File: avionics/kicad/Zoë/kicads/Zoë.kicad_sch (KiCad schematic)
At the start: 52 parts, among them SW1 SW_DIP_x02, X2Y-CAN 4.7nF_X2Y, X2Y-RS485 4.7nF_X2Y

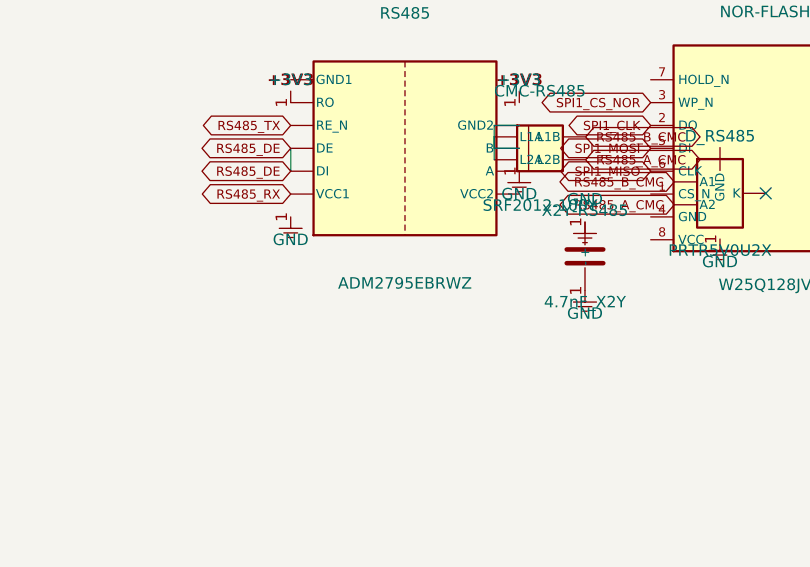
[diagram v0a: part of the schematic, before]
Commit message: Fleet trust module (MCU+TPM+isolated CAN-FD+RS-485) across new CAN-PERIPH-GW-1 board, Jayne, Kaylee, Emma; ISOW1412 swap on Wash/Zoë
- New stackable CAN-PERIPH-GW-1 gateway board (N_STACKS param): MSPM0G3507
  + SLB9670 TPM + ISOW1044BDFMR isolated CAN-FD + ISOW1412 isolated RS-485,
  informed by the public VimDrones ap_periph_pico/ESC S50 concept (no
  VimDrones GPL-3.0 source copied). PCB freerouted via the Specctra DSN/SES
  bridge (tools/export-specctra-dsn.py + import-specctra-ses.py +
  freerouting 2.2.4); user's manual footprint packing preserved.
- Jayne: added ISOW1412 isolated RS-485 (Section H); MSPM0G3507 pinmux
  re-verified against the real datasheet for all new assignments.
- Kaylee: full trust module added via non-destructive schematic injection
  (inject_kaylee_trust_module.py) -- gen_kaylee.py itself has drifted from
  the checked-in file and is not safe to regenerate from (tracked as an
  open item).
- Emma: SLB9670 TPM added via a dedicated header (inject_emma_tpm.py); no
  separate CAN/RS-485 needed, reaches the bus via Zoë's P1/P2 link.
- Fleet-wide ADM2795E -> ISOW1412 (integrated isolated DC-DC). While
  swapping Wash/Zoë, fixed their pre-existing broken ADM2795EBRWZ pin
  numbering and wrong ISOW1044BDFMR footprint (SOIC-16W on a 20-pin part).
- REFERENCES.md: REF-SENSOR-009/010/011 (ISOW1044/ISOW1412/SLB9670),
  ADM2795E supersession, Wash/Zoë defect history, vimdrones GPL note.
- WBS/TODO updated across avionics, airframe/wings-nacelles, and root:
  AK7455 nacelle tilt data is now bus-published by the gateway rather than
  read directly by River/Simon.

Co-Authored-By: Claude Sonnet 5 <noreply@anthropic.com>
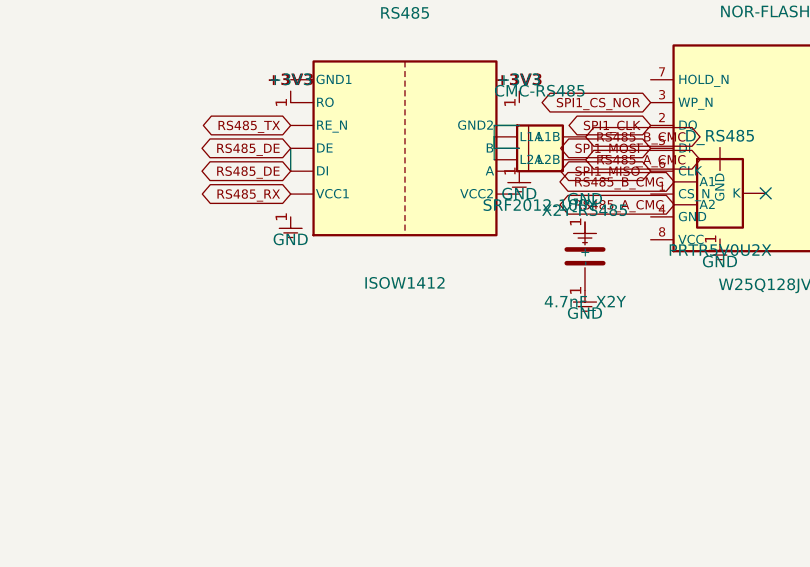
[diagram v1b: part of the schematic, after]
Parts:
- CAN-TR: footprint Package_SO:SOIC-16W_7.5x10.3mm_P1.27mm -> Package_SO:SOIC-20W_7.5x12.8mm_P1.27mm
- RS485: value ADM2795EBRWZ -> ISOW1412; symbol ADM2795EBRWZ -> ISOW1412
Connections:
- net +3V3: now also RS485.4 (RO); no longer RS485.1 (RO)
- net CAN_STB: now also CAN-TR.3 (TXD); no longer CAN-TR.2 (TXD)
- net GND: now also CAN-TR.19 (CANH), RS485.20 (A); no longer CAN-TR.15 (CANH), RS485.19 (A)
- net MCAN1_TX: now also CAN-TR.4 (STB_N); no longer CAN-TR.3 (STB_N)
- net RS485_DE: now also RS485.3 (DE); no longer RS485.4 (DI)
- net RS485_RX: now also RS485.1 (VCC1); no longer RS485.8 (VCC1)
- net RS485_TX: now also RS485.5 (RE_N); no longer RS485.3 (RE_N)
- net at CMC-CAN.1 (L1A), CMC-CAN.2 (L2A): now also CAN-TR.11 (ISOGND), CAN-TR.18 (CANL); no longer CAN-TR.10 (ISOGND), CAN-TR.14 (CANL)
- net at CMC-RS485.1 (L1A), CMC-RS485.2 (L2A): now also RS485.11 (GND2), RS485.19 (B); no longer RS485.12 (GND2), RS485.18 (B)
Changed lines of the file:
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@@
     (property "Value" "ISOW1044BDFMR" (at 210.00 185.00 0)
       (effects (font (size 1.27 1.27))))
-    (property "Footprint" "Package_SO:SOIC-16W_7.5x10.3mm_P1.27mm" (at 0 0 0)
+    (property "Footprint" "Package_SO:SOIC-20W_7.5x12.8mm_P1.27mm" (at 0 0 0)
       (effects (font (size 1.27 1.27)) (hide yes)))
     (property "Datasheet" "https://www.ti.com/lit/ds/symlink/isow1044.pdf" (at 0 0 0)
       (effects (font (size 1.27 1.27)) (hide yes)))
     (pin "1")
-    (pin "2")
     (pin "3")
     (pin "4")
-    (pin "6")
+    (pin "5")
     (pin "10")
     (pin "11")
-    (pin "14")
-    (pin "15")
+    (pin "12")
+    (pin "18")
+    (pin "19")
   )
   (symbol (lib_id "+3V3") (at 197.30 164.92 0)
@@
   (wire (pts (xy 219.92 170.00) (xy 219.92 168.73))
 )
-  (symbol (lib_id "ADM2795EBRWZ") (at 340.00 170.00 0)
+  (symbol (lib_id "ISOW1412") (at 340.00 170.00 0)
     (unit 1) (exclude_from_sim no) (in_bom yes) (on_board yes) (dnp no)
     (property "Reference" "RS485" (at 340.00 155.00 0)
       (effects (font (size 1.27 1.27))))
-    (property "Value" "ADM2795EBRWZ" (at 340.00 185.00 0)
+    (property "Value" "ISOW1412" (at 340.00 185.00 0)
       (effects (font (size 1.27 1.27))))
     (property "Footprint" "Package_SO:SOIC-20W_7.5x12.8mm_P1.27mm" (at 0 0 0)
       (effects (font (size 1.27 1.27)) (hide yes)))
-    (property "Datasheet" "https://www.analog.com/media/en/technical-documentation/data-sheets/ADM2795E.pdf" (at 0 0 0)
+    (property "Datasheet" "https://www.ti.com/lit/ds/symlink/isow1412.pdf" (at 0 0 0)
       (effects (font (size 1.27 1.27)) (hide yes)))
     (pin "1")
@@
     (pin "4")
     (pin "5")
-    (pin "8")
+    (pin "10")
+    (pin "11")
     (pin "12")
-    (pin "16")
-    (pin "18")
     (pin "19")
+    (pin "20")
   )
   (symbol (lib_id "+3V3") (at 327.30 164.92 0)
